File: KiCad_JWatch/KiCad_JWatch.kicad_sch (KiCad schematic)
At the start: 19 parts, among them IC1 BMP390, IC2 BH1750FVI-TR, J1 Conn_01x04_Pin, U1 ESP32-S3-MINI-1, U2 RV-3028-C7, U3 LSM6DS3

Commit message: added heart sensor & hub
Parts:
- removed U1: ESP32-S3-MINI-1, RF_Module:ESP32-S2-MINI-1, symbol RF_Module:ESP32-S3-MINI-1
- added C10, C9: 4.7u, symbol Device:C
- added C11, C15: 1u, symbol Device:C
- added C12: 100n, symbol Device:C
- added C13, C14, C19, C8: 100nF, symbol Device:C
- added C16: 22u, symbol Device:C
- added C17, C18: 8.2p, symbol Device:C
- added IC3: MAX32664GWEA+T, BGA16C35P4X4_157X155X69, symbol MAX32664GWEA+T:MAX32664GWEA+T
- added IC4: MAX30101EFD+T, 14-LEAD-OESIP, symbol MAX30101EFD+T:MAX30101EFD+T
- added J2, J3: Conn_01x07_Pin, symbol Connector:Conn_01x07_Pin
- added NT1: NetTie_2, symbol Device:NetTie_2
- added R10, R11, R12, R9: 2.2k, symbol Device:R
- added R13, R14, R16, R17: 10k, symbol Device:R
- added R15, R8: 200k, symbol Device:R
- added R5, R6: 4.7k, symbol Device:R
- added R7: 10, symbol Device:R
- added U1, U5: PCA9306, symbol Interface:PCA9306
- added U4: ESP32-S3-WROOM-1, RF_Module:ESP32-S3-WROOM-1, symbol RF_Module:ESP32-S3-WROOM-1
- added Y1: 32.768kHz 6pF, symbol Device:Crystal
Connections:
- net IMU_CS is gone; now on net +3.3V: U3.12 (CS)
- net +3.3V: now also C16.1, C19.1, C8.1, C9.1, IC4.10 (VLED+_2), IC4.9 (VLED+_1), J2.2 (Pin_2), J3.2 (Pin_2), R11.1, R12.1, R15.1, R16.1, R17.1, R8.1, U4.2 (3V3)
- net GND: now also C19.2, C8.2, J3.3 (Pin_3), NT1.2, U4.1 (GND), U4.40 (GND), U4.41 (GND)
- net SCL: now also J2.4 (Pin_4), J3.4 (Pin_4), R11.2, U1.6 (SCL2), U4.17 (IO9)
- net SDA: now also J2.5 (Pin_5), J3.5 (Pin_5), R12.2, U1.5 (SDA2), U4.12 (IO8)
- new net: C14.1, R15.2, U5.7 (VREF2), U5.8 (EN)
- new net: C11.1, IC3.A4 (VCORE)
- new net: C17.2, IC3.A1 (32KOUT), Y1.1
- new net: C13.1, R8.2, U1.7 (VREF2), U1.8 (EN)
- new net: C18.2, IC3.A2 (32KIN), Y1.2
- new net: C12.2, R7.1
- new net: J3.1 (Pin_1), NT1.1
- new net +1V8: C10.1, C15.1, IC3.A3 (VDD), IC4.11 (VDD), R10.1, R13.1, R14.1, R5.1, R6.1, R9.1, U1.2 (VREF1), U5.2 (VREF1)
- new net ESP_MFIO: J2.6 (Pin_6), J3.6 (Pin_6), R16.2, U5.6 (SCL2)
- new net ESP_RSTN: J2.7 (Pin_7), J3.7 (Pin_7), R17.2, U5.5 (SDA2)
- new net GND1: C10.2, C11.2, C13.2, C14.2, C15.2, C17.1, C18.1, IC3.B2 (VSS), IC4.12 (GND), J2.3 (Pin_3), R7.2, U1.1 (GND), U5.1 (GND)
- new net HR_INT: IC3.C4 (HR_INT), IC4.13 (~{INT})
- new net HR_SCL: IC3.B4 (SENSOR_SCL), IC4.2 (SCL), R5.2
- new net HR_SDA: IC3.B3 (SENSOR_SDA), IC4.3 (SDA), R6.2
- new net HUB_MFIO: IC3.C2 (MFIO), R13.2, U5.3 (SCL1)
- new net HUB_RSTN: C12.1, IC3.B1 (RSTN), R14.2, U5.4 (SDA1)
- new net HUB_SCL: IC3.D1 (SLAVE_SCL), R9.2, U1.3 (SCL1)
- new net HUB_SDA: IC3.D2 (SLAVE_SDA), R10.2, U1.4 (SDA1)
- new net LED_GND: C16.2, C9.2, IC4.4 (PGND), J2.1 (Pin_1)
- no-connect marks 6 -> 16
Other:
- note added: "Accelerometer"
- note added: "ESP32-S3-WROOM-1-N8R8"
- note added: "Heart rate & SPIO2 sensor + HUB + Level Shifters Sub PCB"

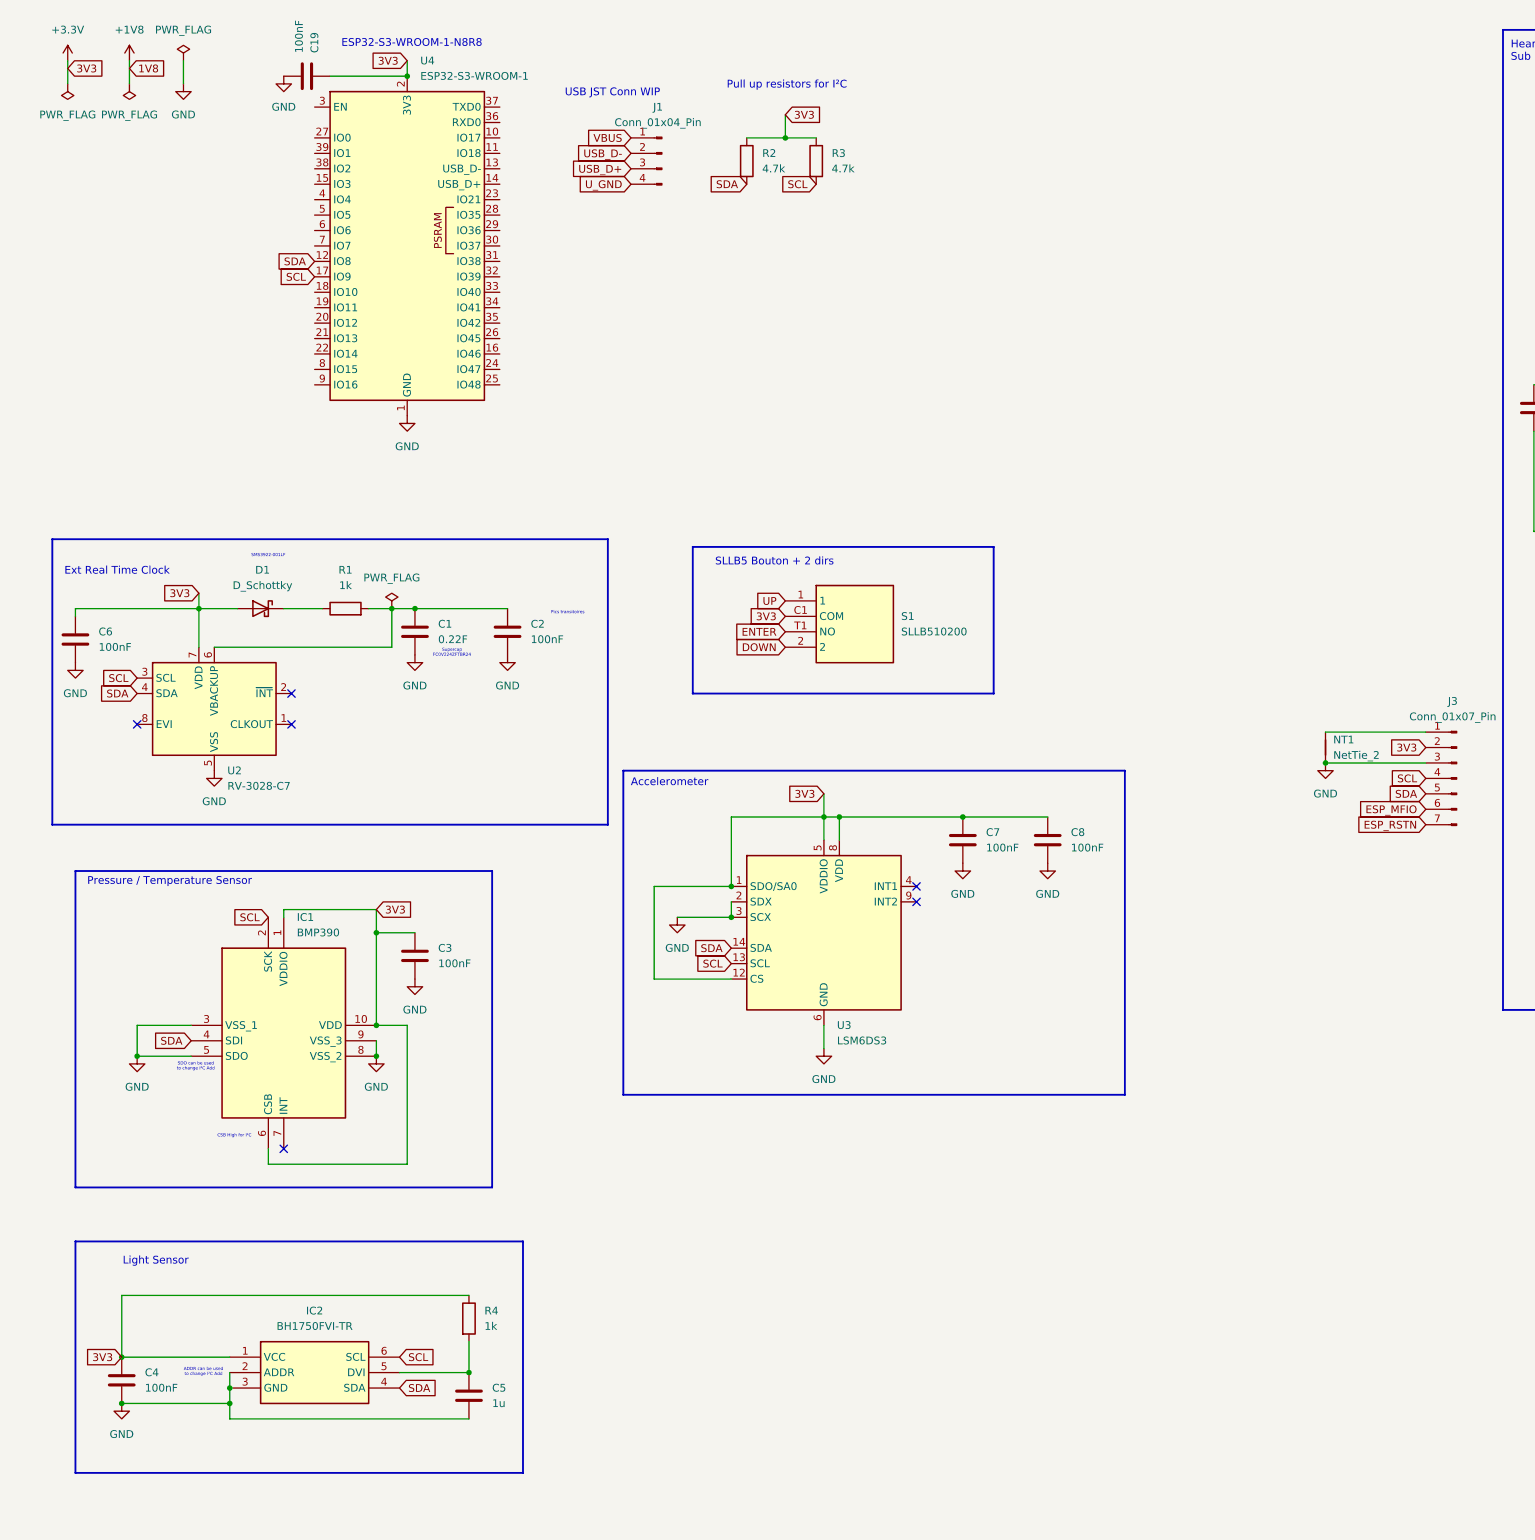
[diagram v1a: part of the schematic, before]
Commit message: startup screen waveshare
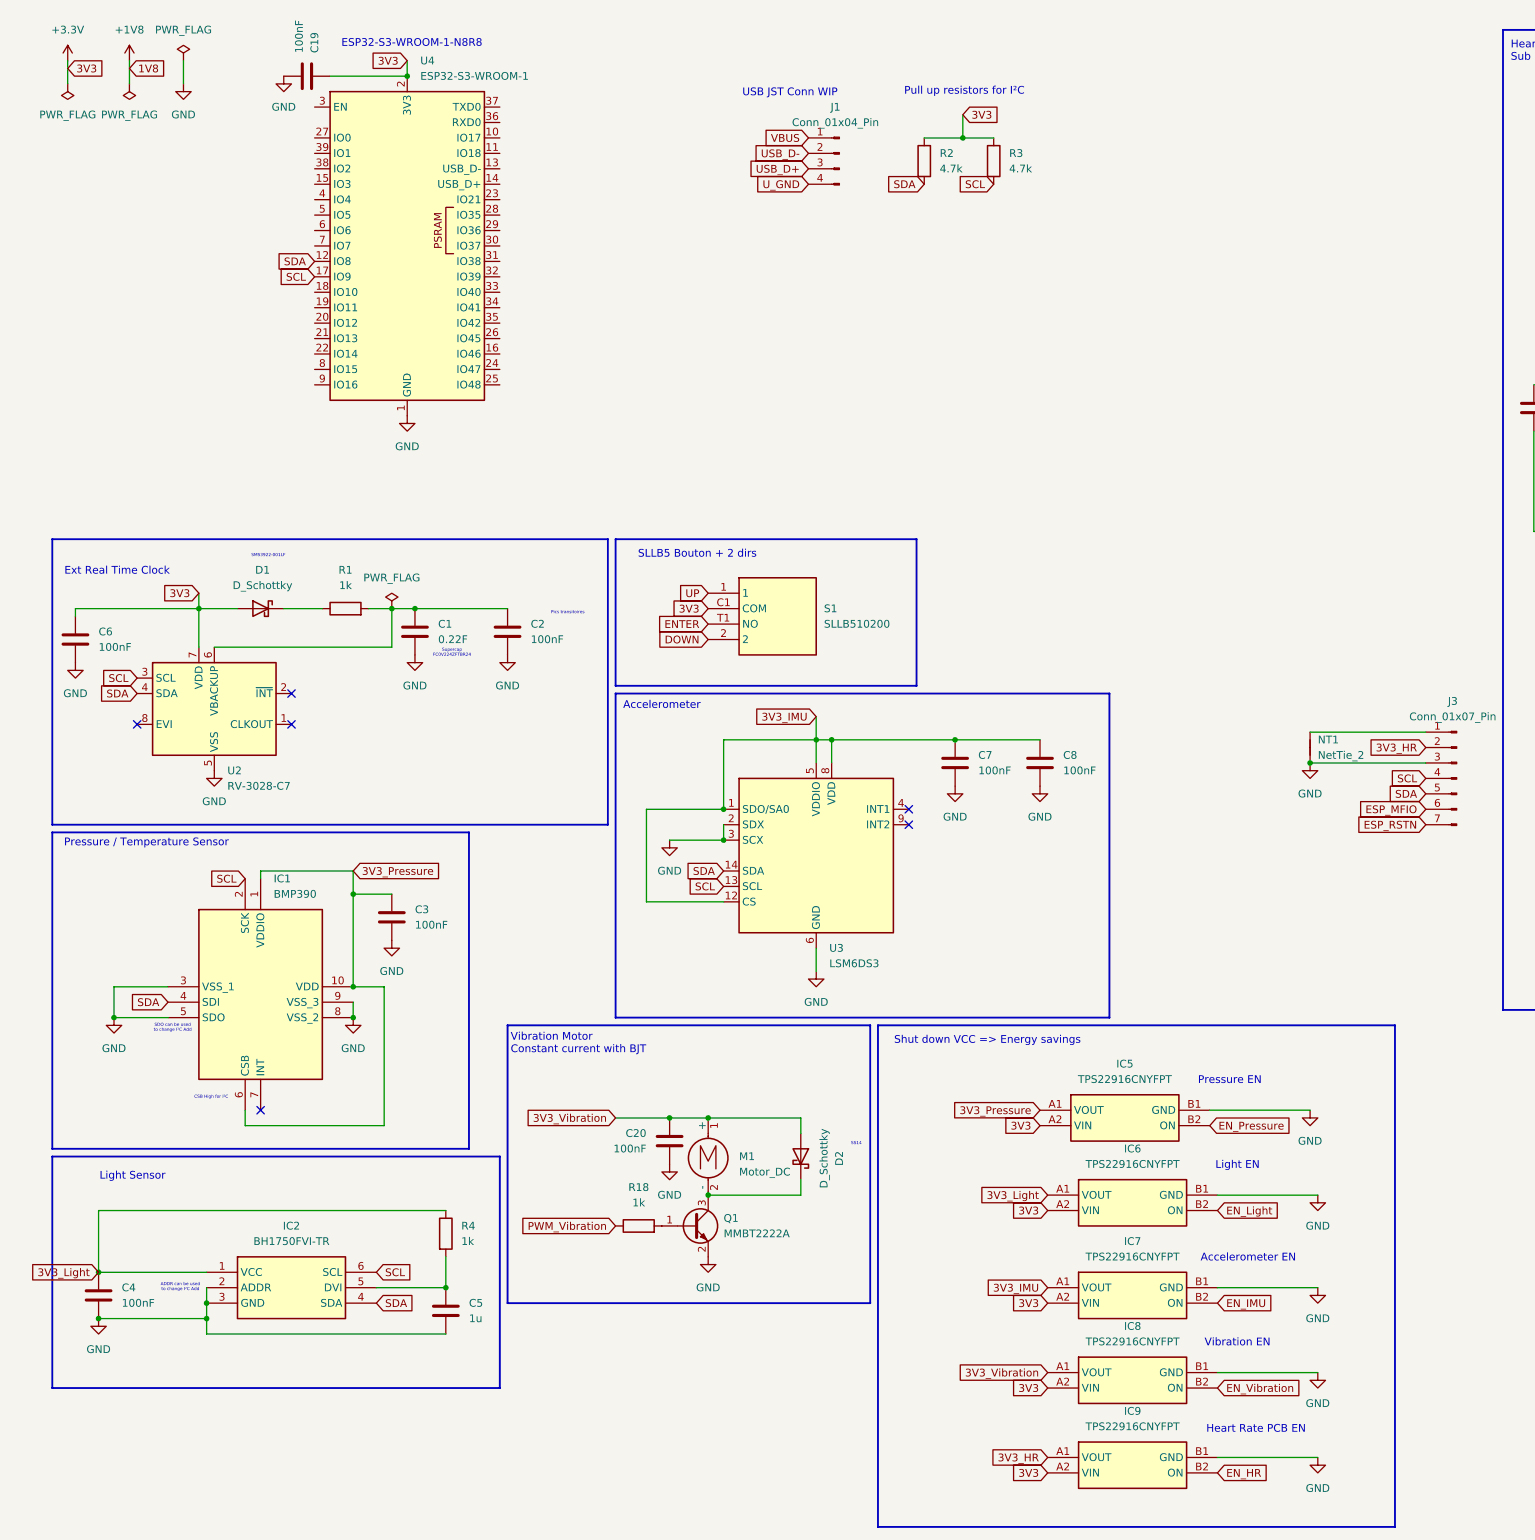
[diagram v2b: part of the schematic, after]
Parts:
- added C20: 100nF, symbol Device:C
- added D2: D_Schottky, symbol Device:D_Schottky
- added IC5, IC6, IC7, IC8, IC9: TPS22916CNYFPT, BGA4C40P2X2_78X78X50, symbol TPS22916CNYFPT:TPS22916CNYFPT
- added M1: Motor_DC, symbol Motor:Motor_DC
- added Q1: MMBT2222A, Package_TO_SOT_SMD:SOT-23, symbol Transistor_BJT:MMBT2222A
- added R18: 1k, symbol Device:R
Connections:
- net +3.3V: now also IC5.A2 (VIN), IC6.A2 (VIN), IC7.A2 (VIN), IC8.A2 (VIN), IC9.A2 (VIN); no longer C3.1, C4.1, C7.1, C8.1, IC1.1 (VDDIO), IC1.10 (VDD), IC1.6 (CSB), IC2.1 (VCC), J3.2 (Pin_2), R4.1, U3.1 (SDO/SA0), U3.12 (CS), U3.5 (VDDIO), U3.8 (VDD)
- net GND: now also C20.2, IC5.B1 (GND), IC6.B1 (GND), IC7.B1 (GND), IC8.B1 (GND), IC9.B1 (GND), Q1.2 (E)
- new net: D2.1 (K), M1.2 (-), Q1.3 (C)
- new net: Q1.1 (B), R18.2
- new net 3V3_HR: IC9.A1 (VOUT), J3.2 (Pin_2)
- new net 3V3_IMU: C7.1, C8.1, IC7.A1 (VOUT), U3.1 (SDO/SA0), U3.12 (CS), U3.5 (VDDIO), U3.8 (VDD)
- new net 3V3_Light: C4.1, IC2.1 (VCC), IC6.A1 (VOUT), R4.1
- new net 3V3_Pressure: C3.1, IC1.1 (VDDIO), IC1.10 (VDD), IC1.6 (CSB), IC5.A1 (VOUT)
- new net 3V3_Vibration: C20.1, D2.2 (A), IC8.A1 (VOUT), M1.1 (+)
- new net EN_HR: IC9.B2 (ON)
- new net EN_IMU: IC7.B2 (ON)
- new net EN_Light: IC6.B2 (ON)
- new net EN_Pressure: IC5.B2 (ON)
- new net EN_Vibration: IC8.B2 (ON)
- new net PWM_Vibration: R18.1
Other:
- note added: "Accelerometer EN"
- note added: "Heart Rate PCB EN"
- note added: "Light EN"
- note added: "Pressure EN"
- note added: "SS14"
- note added: "Shut down VCC => Energy savings"
- note added: "Vibration EN"
- note added: "Vibration Motor Constant current with BJT"
- moved on the sheet: C3, C4, C5, C7, C8, IC1, IC2, J1, NT1, R2, R3, R4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
